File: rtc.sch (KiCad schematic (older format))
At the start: 5 parts, among them J1 Conn_01x05, U1 DS1302N+, Y1 32.768kHz

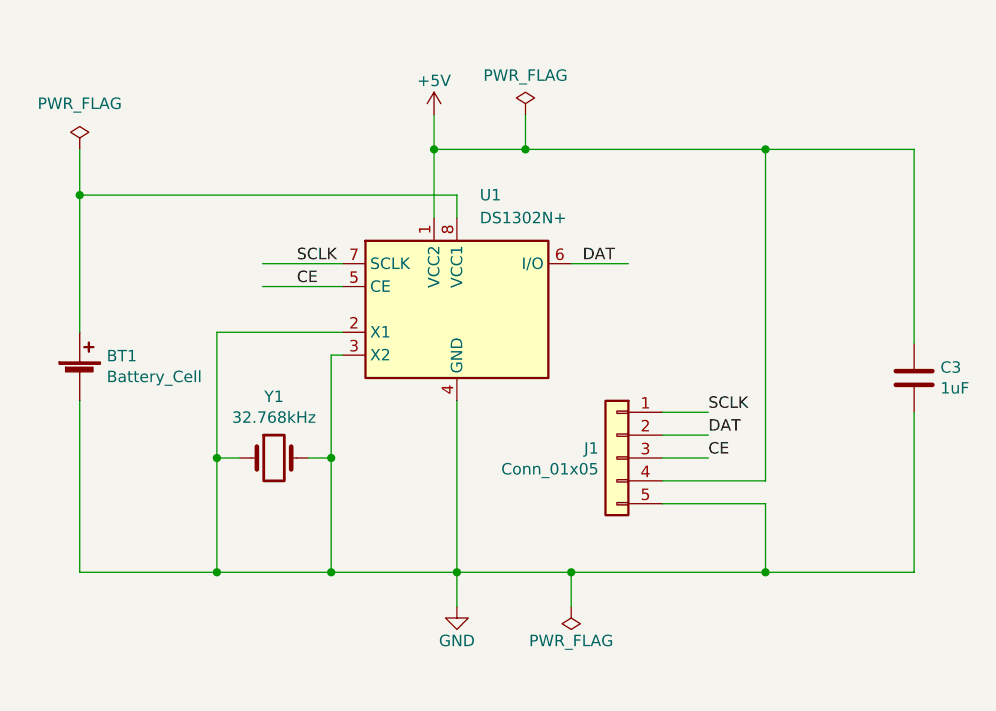
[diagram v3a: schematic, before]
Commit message: Simplify schematic and update readme
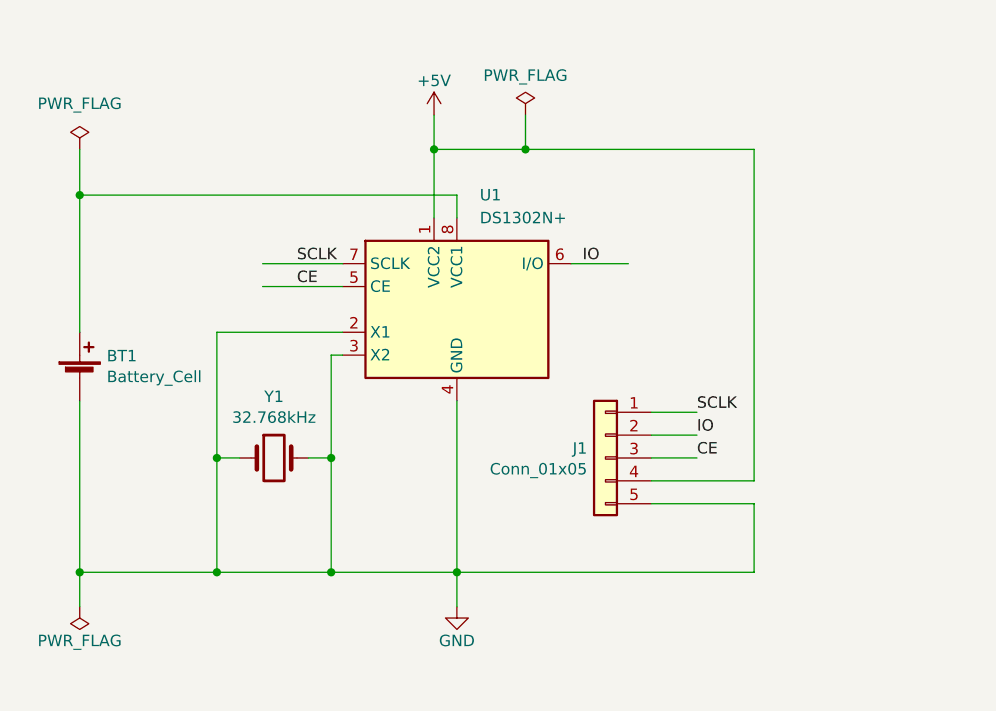
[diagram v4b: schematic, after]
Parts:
- removed C3: 1uF, Capacitor_SMD:C_1206_3216Metric_Pad1.42x1.75mm_HandSolder, symbol rtc-rescue:C-Device
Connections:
- net labels added: IO
- net labels removed: DAT
- wire segments 40 -> 35
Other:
- moved on the sheet: J1
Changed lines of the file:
@@
 L rtc-rescue:Conn_01x05-Connector_Generic J1
 U 1 1 5D86BE0F
-P 3200 2850
-F 0 "J1" H 3280 2892 50  0000 L CNN
-F 1 "Conn_01x05" H 3280 2801 50  0000 L CNN
-F 2 "Connector_PinHeader_2.54mm:PinHeader_1x05_P2.54mm_Vertical" H 3200 2850 50  0001 C CNN
-F 3 "~" H 3200 2850 50  0001 C CNN
-	1    3200 2850
+P 3150 2850
+F 0 "J1" H 3230 2892 50  0000 L CNN
+F 1 "Conn_01x05" H 3230 2801 50  0000 L CNN
+F 2 "Connector_PinHeader_2.54mm:PinHeader_1x05_P2.54mm_Vertical" H 3150 2850 50  0001 C CNN
+F 3 "~" H 3150 2850 50  0001 C CNN
+	1    3150 2850
 	-1   0    0    -1
 $EndComp
@@
 SCLK
 Text Label 3050 2000 0    50   ~ 0
-DAT
+IO
 Text Label 1800 2100 0    50   ~ 0
 CE
 Wire Wire Line
-	3400 2650 3600 2650
+	3350 2650 3550 2650
 Wire Wire Line
-	3400 2750 3600 2750
+	3350 2750 3550 2750
 Wire Wire Line
-	3400 2850 3600 2850
-Text Label 3600 2650 0    50   ~ 0
+	3350 2850 3550 2850
+Text Label 3550 2650 0    50   ~ 0
 SCLK
-Text Label 3600 2750 0    50   ~ 0
-DAT
-Text Label 3600 2850 0    50   ~ 0
+Text Label 3550 2750 0    50   ~ 0
+IO
+Text Label 3550 2850 0    50   ~ 0
 CE
 Wire Wire Line
-	3400 2950 3850 2950
+	3350 2950 3800 2950
 Wire Wire Line
-	3850 3050 3850 3350
+	3800 3050 3800 3350
 Wire Wire Line
-	3400 3050 3850 3050
+	3350 3050 3800 3050
 Connection ~ 2500 3350
 $Comp
@@
 L rtc-rescue:PWR_FLAG-power #FLG0102
 U 1 1 5D89F02D
-P 3000 3500
-F 0 "#FLG0102" H 3000 3575 50  0001 C CNN
-F 1 "PWR_FLAG" H 3000 3650 50  0000 C CNN
-F 2 "" H 3000 3500 50  0001 C CNN
-F 3 "~" H 3000 3500 50  0001 C CNN
-	1    3000 3500
+P 850 3500
+F 0 "#FLG0102" H 850 3575 50  0001 C CNN
+F 1 "PWR_FLAG" H 850 3650 50  0000 C CNN
+F 2 "" H 850 3500 50  0001 C CNN
+F 3 "~" H 850 3500 50  0001 C CNN
+	1    850  3500
 	-1   0    0    1
 $EndComp
 Wire Wire Line
-	3000 3500 3000 3350
+	850  3500 850  3350
 Wire Wire Line
 	2500 3500 2500 3350
-$Comp
-L rtc-rescue:C-Device C3
-U 1 1 5D8CE867
-P 4500 2500
-F 0 "C3" H 4615 2546 50  0000 L CNN
-F 1 "1uF" H 4615 2455 50  0000 L CNN
-F 2 "Capacitor_SMD:C_1206_3216Metric_Pad1.42x1.75mm_HandSolder" H 4538 2350 50  0001 C CNN
-F 3 "~" H 4500 2500 50  0001 C CNN
-	1    4500 2500
-	1    0    0    -1
-$EndComp
 Wire Wire Line
 	2500 1800 2500 1700
@@
 	850  1700 850  2300
 Wire Wire Line
-	3850 1500 3850 2950
+	3800 1500 3800 2950
 Wire Wire Line
 	2400 1500 2400 1800
@@
 	1    0    0    -1
 $EndComp
-Wire Wire Line
-	4500 3350 3850 3350
-Wire Wire Line
-	4500 2650 4500 3350
-Connection ~ 3850 3350
-Wire Wire Line
-	4500 1500 3850 1500
-Wire Wire Line
-	4500 1500 4500 2350
-Connection ~ 3850 1500
-Connection ~ 3000 3350
-Wire Wire Line
-	3000 3350 3850 3350
-Wire Wire Line
-	2500 3350 3000 3350
 Connection ~ 2400 1500
 Connection ~ 1450 2850
@@
 Wire Wire Line
 	2400 1500 2800 1500
-Wire Wire Line
-	2800 1500 3850 1500
 $Comp
 L rtc-rescue:PWR_FLAG-power #FLG0101
@@
 	1    0    0    -1
 $EndComp
+Wire Wire Line
+	2800 1500 3800 1500
+Connection ~ 850  3350
+Wire Wire Line
+	2500 3350 3800 3350
 $EndSCHEMATC

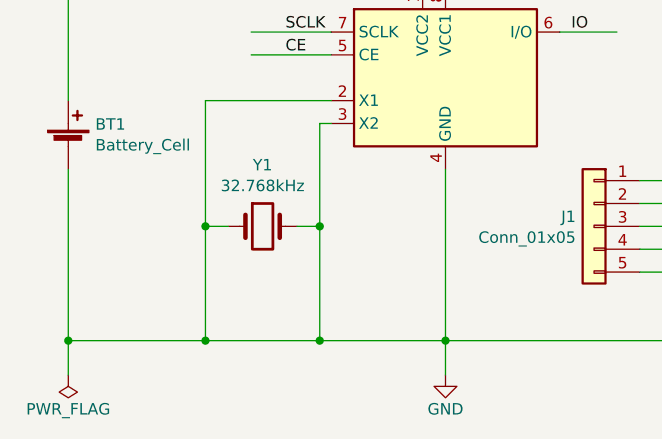
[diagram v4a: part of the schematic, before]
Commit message: Simplify by removing pull-ups and bypass cap per datasheet
- Re-run traces
- Update img/readme
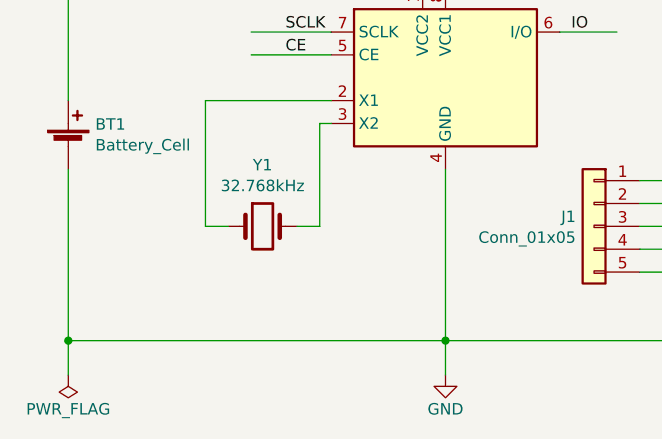
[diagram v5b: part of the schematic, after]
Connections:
- wire segments 35 -> 31
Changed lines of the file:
@@
 	1850 2850 1950 2850
-Wire Wire Line
-	1450 3350 1950 3350
-Connection ~ 1950 3350
-Wire Wire Line
-	1950 3350 2500 3350
 Wire Wire Line
 	2500 2600 2500 3350
@@
 	-1   0    0    -1
 $EndComp
-Connection ~ 1450 3350
-Wire Wire Line
-	850  3350 1450 3350
 Wire Wire Line
 	1650 2000 2000 2000
@@
 $EndComp
 Connection ~ 2400 1500
-Connection ~ 1450 2850
-Wire Wire Line
-	1450 2850 1450 3350
-Connection ~ 1950 2850
-Wire Wire Line
-	1950 2850 1950 3350
 Wire Wire Line
 	1450 2300 1450 2850
@@
 Wire Wire Line
 	2500 3350 3800 3350
+Wire Wire Line
+	850  3350 2500 3350
 $EndSCHEMATC

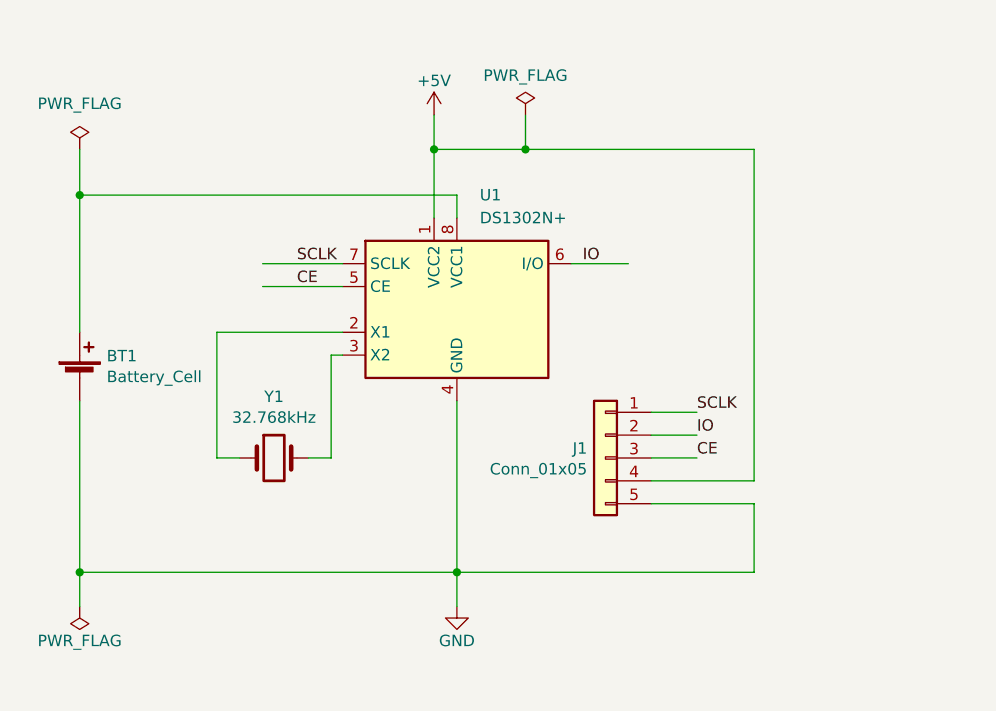
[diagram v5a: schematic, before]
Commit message: Update schematic labels and associate footprints with new digikey component selections
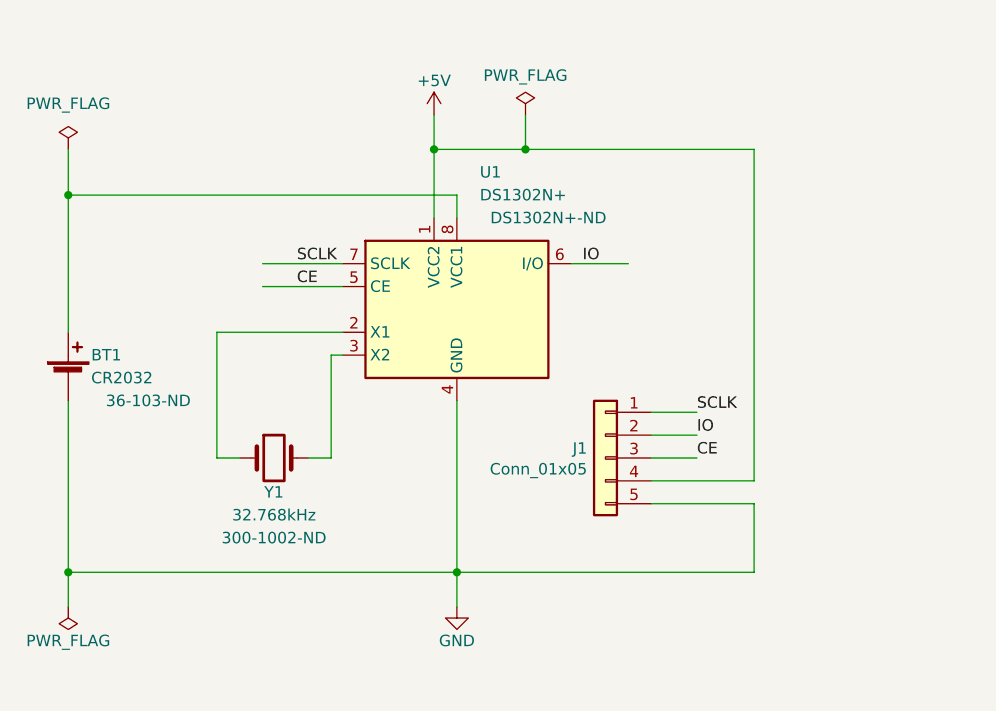
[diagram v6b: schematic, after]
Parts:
- BT1: value Battery_Cell -> CR2032; footprint Battery:BatteryHolder_Keystone_1060_1x2032 -> Battery:BatteryHolder_Keystone_103_1x20mm; digikey (none) -> 36-103-ND
- J1: footprint Connector_PinHeader_2.54mm:PinHeader_1x05_P2.54mm_Vertical -> Connector_PinHeader_2.54mm:PinHeader_1x05_P2.54mm_Horizontal
- U1: digikey (none) -> DS1302N+-ND
- Y1: footprint Crystal:Crystal_HC49-U_Vertical -> Crystal:Crystal_Round_D2.0mm_Vertical; digikey (none) -> 300-1002-ND
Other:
- moved on the sheet: BT1
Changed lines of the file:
@@
 Comment4 ""
 $EndDescr
-$Comp
-L rtc-rescue:DS1302N+-Timer_RTC U1
-U 1 1 5D85BF93
-P 2500 2200
-F 0 "U1" H 2600 2700 50  0000 L CNN
-F 1 "DS1302N+" H 2600 2600 50  0000 L CNN
-F 2 "Package_DIP:DIP-8_W7.62mm" H 2500 1700 50  0001 C CNN
-F 3 "https://datasheets.maximintegrated.com/en/ds/DS1302.pdf" H 2500 2000 50  0001 C CNN
-	1    2500 2200
-	1    0    0    -1
-$EndComp
-$Comp
-L rtc-rescue:Crystal-Device Y1
-U 1 1 5D85EEF2
-P 1700 2850
-F 0 "Y1" H 1700 3118 50  0000 C CNN
-F 1 "32.768kHz" H 1700 3027 50  0000 C CNN
-F 2 "Crystal:Crystal_HC49-U_Vertical" H 1700 2850 50  0001 C CNN
-F 3 "~" H 1700 2850 50  0001 C CNN
-	1    1700 2850
-	1    0    0    -1
-$EndComp
 Wire Wire Line
 	2000 2300 1450 2300
@@
 F 0 "J1" H 3230 2892 50  0000 L CNN
 F 1 "Conn_01x05" H 3230 2801 50  0000 L CNN
-F 2 "Connector_PinHeader_2.54mm:PinHeader_1x05_P2.54mm_Vertical" H 3150 2850 50  0001 C CNN
+F 2 "Connector_PinHeader_2.54mm:PinHeader_1x05_P2.54mm_Horizontal" H 3150 2850 50  0001 C CNN
 F 3 "~" H 3150 2850 50  0001 C CNN
 	1    3150 2850
@@
 L rtc-rescue:Battery_Cell-Device BT1
 U 1 1 5D892343
-P 850 2500
-F 0 "BT1" H 968 2596 50  0000 L CNN
-F 1 "Battery_Cell" H 968 2505 50  0000 L CNN
-F 2 "Battery:BatteryHolder_Keystone_1060_1x2032" V 850 2560 50  0001 C CNN
-F 3 "~" V 850 2560 50  0001 C CNN
-	1    850  2500
+P 800 2500
+F 0 "BT1" H 900 2600 50  0000 L CNN
+F 1 "CR2032" H 900 2500 50  0000 L CNN
+F 2 "Battery:BatteryHolder_Keystone_103_1x20mm" V 800 2560 50  0001 C CNN
+F 3 "~" V 800 2560 50  0001 C CNN
+F 4 "36-103-ND" H 1150 2400 50  0000 C CNN "digikey"
+	1    800  2500
 	1    0    0    -1
 $EndComp
-Wire Wire Line
-	850  3350 850  2600
 Wire Wire Line
 	3000 2000 3250 2000
@@
 L rtc-rescue:PWR_FLAG-power #FLG0102
 U 1 1 5D89F02D
-P 850 3500
-F 0 "#FLG0102" H 850 3575 50  0001 C CNN
-F 1 "PWR_FLAG" H 850 3650 50  0000 C CNN
-F 2 "" H 850 3500 50  0001 C CNN
-F 3 "~" H 850 3500 50  0001 C CNN
-	1    850  3500
+P 800 3500
+F 0 "#FLG0102" H 800 3575 50  0001 C CNN
+F 1 "PWR_FLAG" H 800 3650 50  0000 C CNN
+F 2 "" H 800 3500 50  0001 C CNN
+F 3 "~" H 800 3500 50  0001 C CNN
+	1    800  3500
 	-1   0    0    1
 $EndComp
-Wire Wire Line
-	850  3500 850  3350
 Wire Wire Line
 	2500 3500 2500 3350
 Wire Wire Line
 	2500 1800 2500 1700
-Wire Wire Line
-	850  1700 850  2300
 Wire Wire Line
 	3800 1500 3800 2950
@@
 Wire Wire Line
 	2800 1350 2800 1500
-Connection ~ 850  1700
 Wire Wire Line
-	2500 1700 850  1700
-Wire Wire Line
-	850  1500 850  1700
+	2500 1700 800  1700
 $Comp
 L rtc-rescue:PWR_FLAG-power #FLG0103
 U 1 1 5D8A4FC6
-P 850 1500
-F 0 "#FLG0103" H 850 1575 50  0001 C CNN
-F 1 "PWR_FLAG" H 850 1700 50  0000 C CNN
-F 2 "" H 850 1500 50  0001 C CNN
-F 3 "~" H 850 1500 50  0001 C CNN
-	1    850  1500
+P 800 1500
+F 0 "#FLG0103" H 800 1575 50  0001 C CNN
+F 1 "PWR_FLAG" H 800 1700 50  0000 C CNN
+F 2 "" H 800 1500 50  0001 C CNN
+F 3 "~" H 800 1500 50  0001 C CNN
+	1    800  1500
 	1    0    0    -1
 $EndComp
 Wire Wire Line
 	2800 1500 3800 1500
-Connection ~ 850  3350
 Wire Wire Line
 	2500 3350 3800 3350
 Wire Wire Line
-	850  3350 2500 3350
+	800  3350 2500 3350
+Wire Wire Line
+	800  1500 800  1700
+Connection ~ 800  1700
+Wire Wire Line
+	800  1700 800  2300
+Wire Wire Line
+	800  2600 800  3350
+Connection ~ 800  3350
+Wire Wire Line
+	800  3350 800  3500
+$Comp
+L rtc-rescue:Crystal-Device Y1
+U 1 1 5D85EEF2
+P 1700 2850
+F 0 "Y1" H 1700 2700 50  0000 C CNN
+F 1 "32.768kHz" H 1700 2600 50  0000 C CNN
+F 2 "Crystal:Crystal_Round_D2.0mm_Vertical" H 1700 2850 50  0001 C CNN
+F 3 "~" H 1700 2850 50  0001 C CNN
+F 4 "300-1002-ND" H 1700 2500 50  0000 C CNN "digikey"
+	1    1700 2850
+	1    0    0    -1
+$EndComp
+$Comp
+L rtc-rescue:DS1302N+-Timer_RTC U1
+U 1 1 5D85BF93
+P 2500 2200
+F 0 "U1" H 2600 2800 50  0000 L CNN
+F 1 "DS1302N+" H 2600 2700 50  0000 L CNN
+F 2 "Package_DIP:DIP-8_W7.62mm" H 2500 1700 50  0001 C CNN
+F 3 "https://datasheets.maximintegrated.com/en/ds/DS1302.pdf" H 2500 2000 50  0001 C CNN
+F 4 "DS1302N+-ND" H 2900 2600 50  0000 C CNN "digikey"
+	1    2500 2200
+	1    0    0    -1
+$EndComp
 $EndSCHEMATC

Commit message: Fix courtyard drc error on keystone 103 holder
- fix outline on keystone 103 battery holder and move fixed part into
rtc.pretty
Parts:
- BT1: footprint Battery:BatteryHolder_Keystone_103_1x20mm -> rtc:BatteryHolder_Keystone_103_1x20mm
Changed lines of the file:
@@
 F 0 "BT1" H 900 2600 50  0000 L CNN
 F 1 "CR2032" H 900 2500 50  0000 L CNN
-F 2 "Battery:BatteryHolder_Keystone_103_1x20mm" V 800 2560 50  0001 C CNN
+F 2 "rtc:BatteryHolder_Keystone_103_1x20mm" V 800 2560 50  0001 C CNN
 F 3 "~" V 800 2560 50  0001 C CNN
 F 4 "36-103-ND" H 1150 2400 50  0000 C CNN "digikey"
